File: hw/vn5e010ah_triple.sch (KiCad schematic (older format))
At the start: 6 parts, among them U1201 VN5E010AH, U1202 VN5E010AH

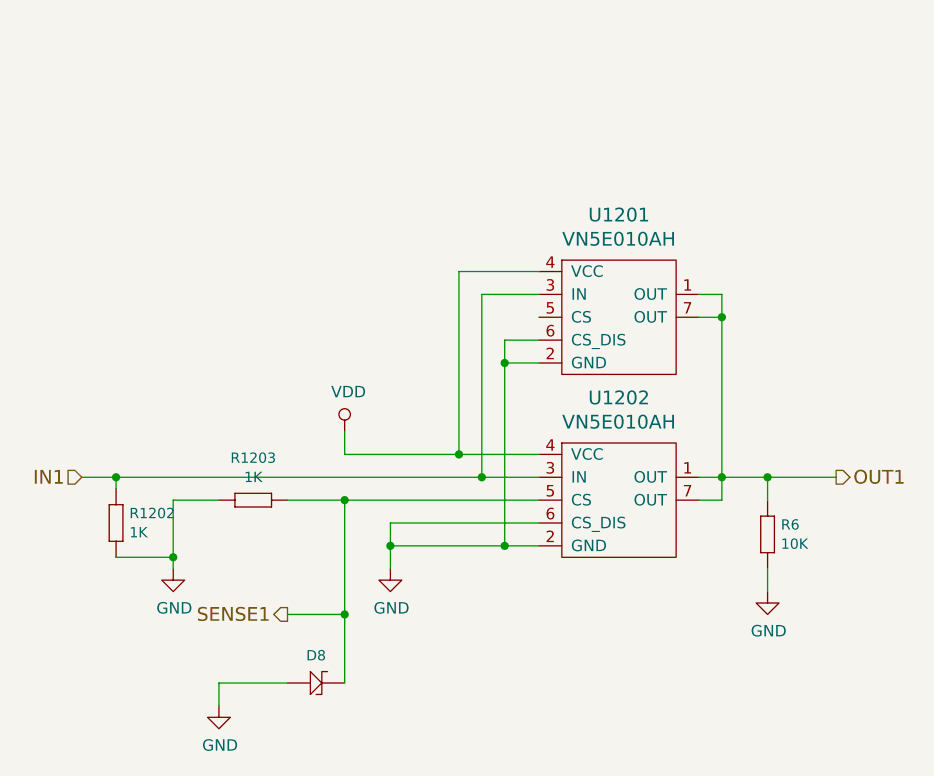
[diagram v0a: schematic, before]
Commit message: reorganazing pcb with 4 fets on radiator
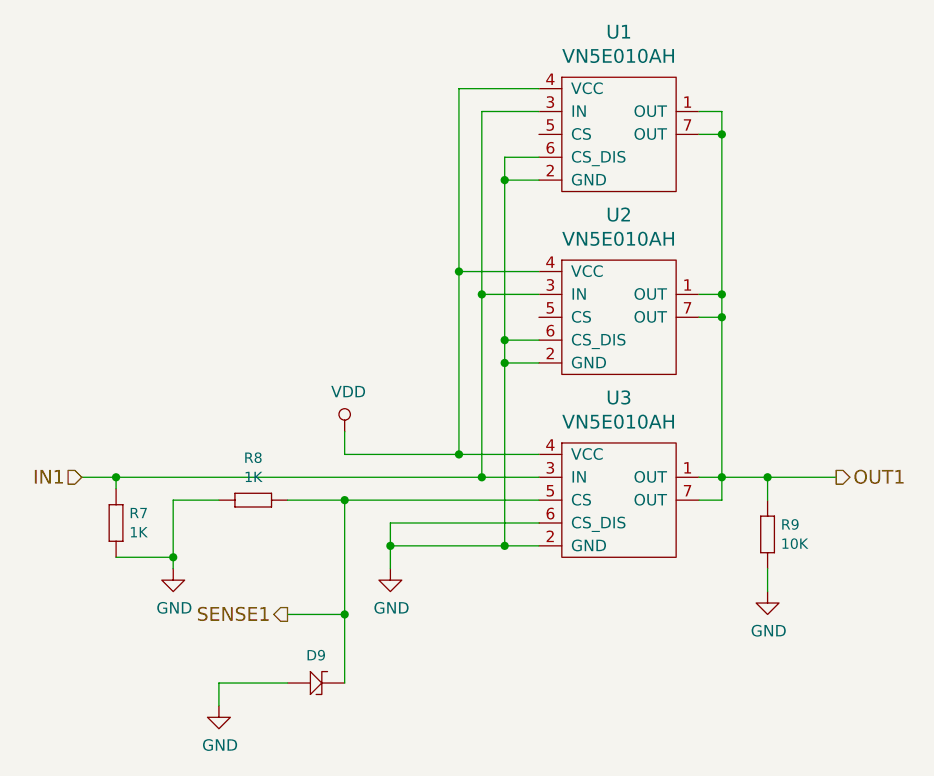
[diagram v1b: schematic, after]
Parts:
- added U1: VN5E010AH, usevolt:HPAK, symbol usevolt:VN5E010AH
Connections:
- net GND: now also U1.2 (GND), U1.6 (CS_DIS)
- net IN1: now also U1.3 (IN)
- net OUT1: now also U1.1 (OUT), U1.7 (OUT)
- net VDD: now also U1.4 (VCC)
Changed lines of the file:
@@
 $Comp
 L power:VDD #PWR01203
-U 1 1 5B1A4079
+U 1 1 5E003D7B
 P 5450 3300
-AR Path="/5B1A3D6E/5B1A4079" Ref="#PWR01203"  Part="1"
-AR Path="/5A13680F/5B1A4079" Ref="#PWR01103"  Part="1"
-AR Path="/5C202EB2/5B1A4079" Ref="#PWR0104"  Part="1"
-F 0 "#PWR01203" H 5450 3150 50  0001 C CNN
+AR Path="/5B1A3D6E/5E003D7B" Ref="#PWR01203"  Part="1"
+AR Path="/5A13680F/5E003D7B" Ref="#PWR01103"  Part="1"
+AR Path="/5C202EB2/5E003D7B" Ref="#PWR0104"  Part="1"
+F 0 "#PWR0104" H 5450 3150 50  0001 C CNN
 F 1 "VDD" H 5467 3473 50  0000 C CNN
 F 2 "" H 5450 3300 50  0000 C CNN
@@
 $Comp
 L power:GND #PWR01201
-U 1 1 5B1A4087
+U 1 1 5E003D7C
 P 4700 3900
-AR Path="/5B1A3D6E/5B1A4087" Ref="#PWR01201"  Part="1"
-AR Path="/5A13680F/5B1A4087" Ref="#PWR01101"  Part="1"
-AR Path="/5C202EB2/5B1A4087" Ref="#PWR0105"  Part="1"
-F 0 "#PWR01201" H 4700 3650 50  0001 C CNN
+AR Path="/5B1A3D6E/5E003D7C" Ref="#PWR01201"  Part="1"
+AR Path="/5A13680F/5E003D7C" Ref="#PWR01101"  Part="1"
+AR Path="/5C202EB2/5E003D7C" Ref="#PWR0105"  Part="1"
+F 0 "#PWR0105" H 4700 3650 50  0001 C CNN
 F 1 "GND" H 4705 3727 50  0000 C CNN
 F 2 "" H 4700 3900 50  0000 C CNN
@@
 $Comp
 L yageo:1K R?
-U 1 1 5B1A4092
+U 1 1 5E003D7D
 P 4450 3650
-AR Path="/5A01611C/5B1A4092" Ref="R?"  Part="1"
-AR Path="/5A019746/5B1A4092" Ref="R?"  Part="1"
-AR Path="/5A01A445/5B1A4092" Ref="R?"  Part="1"
-AR Path="/5A01AB59/5B1A4092" Ref="R?"  Part="1"
-AR Path="/5A120DD2/5B1A4092" Ref="R?"  Part="1"
-AR Path="/5A12FF64/5B1A4092" Ref="R?"  Part="1"
-AR Path="/5A130D3E/5B1A4092" Ref="R?"  Part="1"
-AR Path="/5A1349CF/5B1A4092" Ref="R?"  Part="1"
-AR Path="/5A1358B0/5B1A4092" Ref="R?"  Part="1"
-AR Path="/5A13680F/5B1A4092" Ref="R1101"  Part="1"
-AR Path="/5A14370A/5B1A4092" Ref="R?"  Part="1"
-AR Path="/5B1A3D6E/5B1A4092" Ref="R1202"  Part="1"
-AR Path="/5C202EB2/5B1A4092" Ref="R7"  Part="1"
-F 0 "R1202" V 4458 3708 45  0000 L CNN
+AR Path="/5A01611C/5E003D7D" Ref="R?"  Part="1"
+AR Path="/5A019746/5E003D7D" Ref="R?"  Part="1"
+AR Path="/5A01A445/5E003D7D" Ref="R?"  Part="1"
+AR Path="/5A01AB59/5E003D7D" Ref="R?"  Part="1"
+AR Path="/5A120DD2/5E003D7D" Ref="R?"  Part="1"
+AR Path="/5A12FF64/5E003D7D" Ref="R?"  Part="1"
+AR Path="/5A130D3E/5E003D7D" Ref="R?"  Part="1"
+AR Path="/5A1349CF/5E003D7D" Ref="R?"  Part="1"
+AR Path="/5A1358B0/5E003D7D" Ref="R?"  Part="1"
+AR Path="/5A13680F/5E003D7D" Ref="R1101"  Part="1"
+AR Path="/5A14370A/5E003D7D" Ref="R?"  Part="1"
+AR Path="/5B1A3D6E/5E003D7D" Ref="R1202"  Part="1"
+AR Path="/5C202EB2/5E003D7D" Ref="R7"  Part="1"
+F 0 "R7" V 4458 3708 45  0000 L CNN
 F 1 "1K" V 4542 3708 45  0000 L CNN
 F 2 "yageo:0603" H 4480 3800 20  0001 C CNN
@@
 $Comp
 L usevolt:VN5E010AH U1202
-U 1 1 5B1A40AC
+U 1 1 5E003D7E
 P 6700 3600
-AR Path="/5B1A3D6E/5B1A40AC" Ref="U1202"  Part="1"
-AR Path="/5A13680F/5B1A40AC" Ref="U1103"  Part="1"
-AR Path="/5C202EB2/5B1A40AC" Ref="U2"  Part="1"
-F 0 "U1202" H 6650 4047 60  0000 C CNN
+AR Path="/5B1A3D6E/5E003D7E" Ref="U1202"  Part="1"
+AR Path="/5A13680F/5E003D7E" Ref="U1103"  Part="1"
+AR Path="/5C202EB2/5E003D7E" Ref="U3"  Part="1"
+F 0 "U3" H 6650 4047 60  0000 C CNN
 F 1 "VN5E010AH" H 6650 3941 60  0000 C CNN
 F 2 "usevolt:HPAK" H 6350 4550 60  0001 C CNN
@@
 $Comp
 L power:GND #PWR01204
-U 1 1 5B1A40B3
+U 1 1 5E003D7F
 P 5650 3900
-AR Path="/5B1A3D6E/5B1A40B3" Ref="#PWR01204"  Part="1"
-AR Path="/5A13680F/5B1A40B3" Ref="#PWR01104"  Part="1"
-AR Path="/5C202EB2/5B1A40B3" Ref="#PWR0112"  Part="1"
-F 0 "#PWR01204" H 5650 3650 50  0001 C CNN
+AR Path="/5B1A3D6E/5E003D7F" Ref="#PWR01204"  Part="1"
+AR Path="/5A13680F/5E003D7F" Ref="#PWR01104"  Part="1"
+AR Path="/5C202EB2/5E003D7F" Ref="#PWR0112"  Part="1"
+F 0 "#PWR0112" H 5650 3650 50  0001 C CNN
 F 1 "GND" H 5655 3727 50  0000 C CNN
 F 2 "" H 5650 3900 50  0000 C CNN
@@
 $Comp
 L usevolt:VN5E010AH U1201
-U 1 1 5B1A4293
+U 1 1 5E003D80
 P 6700 2800
-AR Path="/5B1A3D6E/5B1A4293" Ref="U1201"  Part="1"
-AR Path="/5A13680F/5B1A4293" Ref="U1102"  Part="1"
-AR Path="/5C202EB2/5B1A4293" Ref="U1"  Part="1"
-F 0 "U1201" H 6650 3247 60  0000 C CNN
+AR Path="/5B1A3D6E/5E003D80" Ref="U1201"  Part="1"
+AR Path="/5A13680F/5E003D80" Ref="U1102"  Part="1"
+AR Path="/5C202EB2/5E003D80" Ref="U2"  Part="1"
+F 0 "U2" H 6650 3247 60  0000 C CNN
 F 1 "VN5E010AH" H 6650 3141 60  0000 C CNN
 F 2 "usevolt:HPAK" H 6350 3750 60  0001 C CNN
@@
 $Comp
 L yageo:1K R1203
-U 1 1 5E003D81
+U 1 1 5B2322BF
 P 5000 3600
-AR Path="/5B1A3D6E/5E003D81" Ref="R1203"  Part="1"
-AR Path="/5A13680F/5E003D81" Ref="R1102"  Part="1"
-AR Path="/5C202EB2/5E003D81" Ref="R8"  Part="1"
-F 0 "R1203" H 5050 3784 45  0000 C CNN
+AR Path="/5B1A3D6E/5B2322BF" Ref="R1203"  Part="1"
+AR Path="/5A13680F/5B2322BF" Ref="R1102"  Part="1"
+AR Path="/5C202EB2/5B2322BF" Ref="R8"  Part="1"
+F 0 "R8" H 5050 3784 45  0000 C CNN
 F 1 "1K" H 5050 3700 45  0000 C CNN
 F 2 "yageo:0603" H 5030 3750 20  0001 C CNN
@@
 $Comp
 L yageo:10K R6
-U 1 1 5BA96DF9
+U 1 1 5E003D82
 P 7300 3700
-AR Path="/5B1A3D6E/5BA96DF9" Ref="R6"  Part="1"
-AR Path="/5A13680F/5BA96DF9" Ref="R5"  Part="1"
-AR Path="/5C202EB2/5BA96DF9" Ref="R9"  Part="1"
-F 0 "R6" V 7308 3758 45  0000 L CNN
+AR Path="/5B1A3D6E/5E003D82" Ref="R6"  Part="1"
+AR Path="/5A13680F/5E003D82" Ref="R5"  Part="1"
+AR Path="/5C202EB2/5E003D82" Ref="R9"  Part="1"
+F 0 "R9" V 7308 3758 45  0000 L CNN
 F 1 "10K" V 7392 3758 45  0000 L CNN
 F 2 "yageo:0603" H 7330 3850 20  0001 C CNN
@@
 $Comp
 L power:GND #PWR0111
-U 1 1 5E003D83
+U 1 1 5BA9746E
 P 7300 4000
-AR Path="/5B1A3D6E/5E003D83" Ref="#PWR0111"  Part="1"
-AR Path="/5A13680F/5E003D83" Ref="#PWR0110"  Part="1"
-AR Path="/5C202EB2/5E003D83" Ref="#PWR0113"  Part="1"
-F 0 "#PWR0111" H 7300 3750 50  0001 C CNN
+AR Path="/5B1A3D6E/5BA9746E" Ref="#PWR0111"  Part="1"
+AR Path="/5A13680F/5BA9746E" Ref="#PWR0110"  Part="1"
+AR Path="/5C202EB2/5BA9746E" Ref="#PWR0113"  Part="1"
+F 0 "#PWR0113" H 7300 3750 50  0001 C CNN
 F 1 "GND" H 7305 3827 50  0000 C CNN
 F 2 "" H 7300 4000 50  0000 C CNN
@@
 $Comp
 L usevolt:ZENER_MM3Z3V6T1G D8
-U 1 1 5E003D84
+U 1 1 5BAAE03B
 P 5400 4400
-AR Path="/5B1A3D6E/5E003D84" Ref="D8"  Part="1"
-AR Path="/5A13680F/5E003D84" Ref="D7"  Part="1"
-AR Path="/5C202EB2/5E003D84" Ref="D9"  Part="1"
-F 0 "D8" H 5325 4520 45  0000 C CNN
+AR Path="/5B1A3D6E/5BAAE03B" Ref="D8"  Part="1"
+AR Path="/5A13680F/5BAAE03B" Ref="D7"  Part="1"
+AR Path="/5C202EB2/5BAAE03B" Ref="D9"  Part="1"
+F 0 "D9" H 5325 4520 45  0000 C CNN
 F 1 "ZENER_MM3Z3V6T1G" H 5675 4775 45  0001 L BNN
 F 2 "usevolt:SOD-323" H 5375 4775 20  0001 C CNN
@@
 $Comp
 L power:GND #PWR0103
-U 1 1 5E003D85
+U 1 1 5BAAE0D6
 P 4900 4500
-AR Path="/5B1A3D6E/5E003D85" Ref="#PWR0103"  Part="1"
-AR Path="/5A13680F/5E003D85" Ref="#PWR0102"  Part="1"
-AR Path="/5C202EB2/5E003D85" Ref="#PWR0114"  Part="1"
-F 0 "#PWR0103" H 4900 4250 50  0001 C CNN
+AR Path="/5B1A3D6E/5BAAE0D6" Ref="#PWR0103"  Part="1"
+AR Path="/5A13680F/5BAAE0D6" Ref="#PWR0102"  Part="1"
+AR Path="/5C202EB2/5BAAE0D6" Ref="#PWR0114"  Part="1"
+F 0 "#PWR0114" H 4900 4250 50  0001 C CNN
 F 1 "GND" H 4905 4327 50  0000 C CNN
 F 2 "" H 4900 4500 50  0000 C CNN
@@
 Wire Wire Line
 	4900 4400 5200 4400
+$Comp
+L usevolt:VN5E010AH U?
+U 1 1 5DFFFA78
+P 6700 2000
+AR Path="/5B1A3D6E/5DFFFA78" Ref="U?"  Part="1"
+AR Path="/5A13680F/5DFFFA78" Ref="U?"  Part="1"
+AR Path="/5C202EB2/5DFFFA78" Ref="U1"  Part="1"
+F 0 "U1" H 6650 2447 60  0000 C CNN
+F 1 "VN5E010AH" H 6650 2341 60  0000 C CNN
+F 2 "usevolt:HPAK" H 6350 2950 60  0001 C CNN
+F 3 "http://www.st.com/content/ccc/resource/technical/document/datasheet/1e/52/ef/e0/cc/90/4e/2e/CD00240716.pdf/files/CD00240716.pdf/jcr:content/translations/en.CD00240716.pdf" H 6450 3050 60  0001 C CNN
+F 4 "STMicroelectronics" H 6550 3150 60  0001 C CNN "Manufacturer"
+F 5 "VN5E010AHTR-E" H 6650 3250 60  0001 C CNN "Manufacturer Part Number"
+F 6 "Digikey" H 6750 3350 60  0001 C CNN "1st Source"
+F 7 "497-10505-2-ND" H 6850 3450 60  0001 C CNN "1st Source Part Number"
+	1    6700 2000
+	1    0    0    -1
+$EndComp
+Wire Wire Line
+	7000 2000 7100 2000
+Wire Wire Line
+	7100 2000 7100 2700
+Connection ~ 7100 2700
+Wire Wire Line
+	7000 1900 7100 1900
+Wire Wire Line
+	7100 1900 7100 2000
+Connection ~ 7100 2000
+Wire Wire Line
+	6300 2200 6150 2200
+Connection ~ 6150 2900
+Wire Wire Line
+	6300 2100 6150 2100
+Wire Wire Line
+	6150 2100 6150 2200
+Connection ~ 6150 2200
+Wire Wire Line
+	6150 2200 6150 2900
+Wire Wire Line
+	6300 1900 6050 1900
+Wire Wire Line
+	6050 1900 6050 2700
+Connection ~ 6050 2700
+Wire Wire Line
+	6300 1800 5950 1800
+Wire Wire Line
+	5950 1800 5950 2600
+Connection ~ 5950 2600
 $EndSCHEMATC
